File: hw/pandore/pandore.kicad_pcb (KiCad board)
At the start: 4 copper layers, 100 x 100 mm, 65 parts, among them U1 LattePanda_Mu, U2 mem_flash_spi, U3 RP2350B, U4 RP2350B, U5 mem_flash_spi, U6 mem_flash_spi

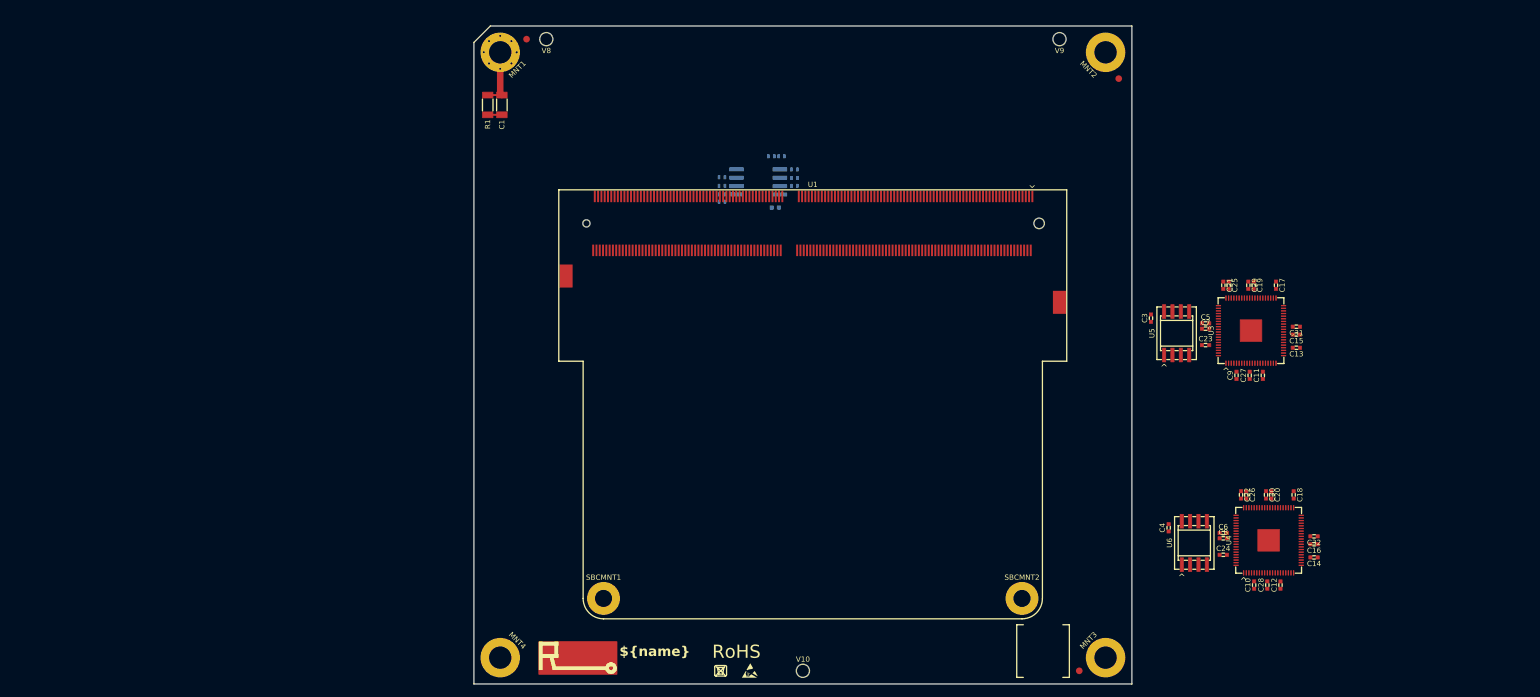
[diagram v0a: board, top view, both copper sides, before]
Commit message: added usb, hdmi and combo xlrtrs connectors resized pcb for something realistic (still wip)
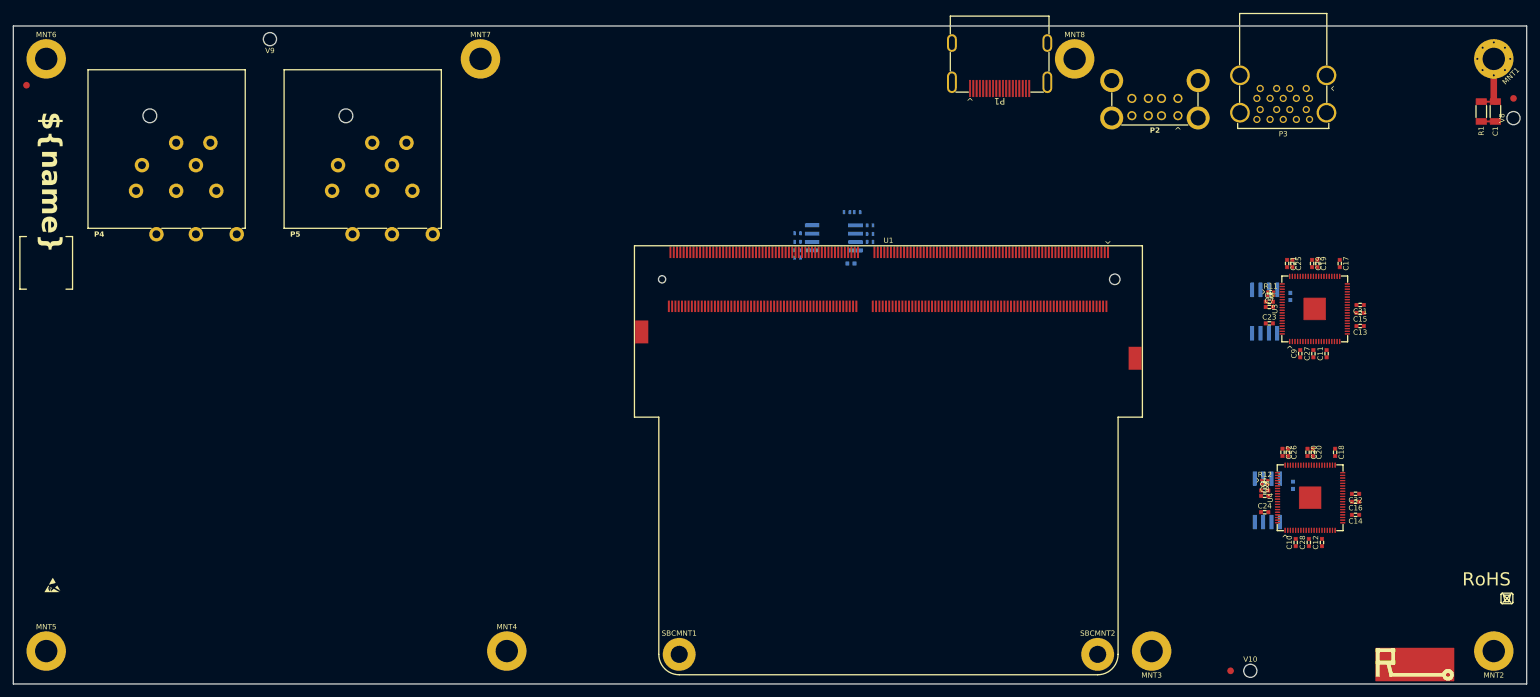
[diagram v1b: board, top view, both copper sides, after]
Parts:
- added MNT5: Mounting, reekilib_mnt:mnt_M3, F.Cu at (35.0, 145.0)
- added MNT6: Mounting, reekilib_mnt:mnt_M3, F.Cu at (35.0, 55.0)
- added MNT7: Mounting, reekilib_mnt:mnt_M3, F.Cu at (101.0, 55.0)
- added MNT8: Mounting, reekilib_mnt:mnt_M3, F.Cu at (191.3, 55.0)
- added P1: HDMI, reekilib_con:TE_1747981-1, F.Cu at (179.9, 54.6)
- added P2: USB2-A_2stacked, reekilib_con:USB2_A_RCPT_HORZ_2STACKED, F.Cu at (203.5, 58.3)
- added P3: USB3-A_2stacked, reekilib_con:USB3_A_RCPT_HORZ_2STACKED, F.Cu at (223.0, 57.5)
- added P4: XLR+TRS6.35+SW, reekilib_con:neutrik_ncj9fi-h-0, F.Cu at (54.8, 75.0)
- added P5: XLR+TRS6.35+SW, reekilib_con:neutrik_ncj9fi-h-0, F.Cu at (84.5, 75.0)
- added R11: 27Ω, 5%, 63mW, reekilib_res:RESCAXSR65P100X100X35-4, F.Cu at (221.1, 90.7)
- added R12: 27Ω, 5%, 63mW, reekilib_res:RESCAXSR65P100X100X35-4, F.Cu at (220.2, 119.3)
- C3, C4, U5, U6: moved to B.Cu
- moved V6 166.0 mm to (32.0, 59.0)
- moved V11 162.6 mm to (35.0, 86.0)
- moved C1 151.0 mm to (255.2, 63.0)
- moved MNT1 151.0 mm to (255.0, 55.0)
- moved R1 151.0 mm to (253.1, 63.0)
- moved V5 150.3 mm to (258.0, 61.0), turned to -90 degrees
- moved V8 147.5 mm to (258.0, 64.0), turned to -90 degrees
- moved V1 127.2 mm to (243.0, 147.0)
- moved V3 120.0 mm to (257.0, 137.0)
- moved V9 120.0 mm to (69.0, 52.0)
- moved V2 114.5 mm to (254.0, 134.0)
- moved MNT2 108.5 mm to (255.0, 145.0), turned to 45 degrees
- moved V4 106.8 mm to (36.0, 135.0)
- moved V10 68.0 mm to (218.0, 148.0)
- moved V7 23.0 mm to (215.0, 148.0)
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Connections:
- U3 pad 66: unconnected-(U3B-USB.D-|USB-Pad66) -> /Mgmt MCU/MCU/_USB.D-
- U3 pad 67: unconnected-(U3B-USB.D+|USB-Pad67) -> /Mgmt MCU/MCU/_USB.D+
- U4 pad 66: unconnected-(U4B-USB.D-|USB-Pad66) -> /Real-Time MCU/MCU/_USB.D-
- U4 pad 67: unconnected-(U4B-USB.D+|USB-Pad67) -> /Real-Time MCU/MCU/_USB.D+
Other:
- board size 100 x 100 mm -> 230 x 100 mm

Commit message: added RP2350's crystals added 8p8c shielded with led connector (both the same for now)
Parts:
- added J1: 8p8c_2led_shield, reekilib_con:amphenol_RJE58-188-54x1-0x, F.Cu at (160.0, 61.0)
- added J2: 8p8c_2led_shield, reekilib_con:amphenol_RJE58-188-54x1-0x, F.Cu at (140.0, 61.0)
- added X1: 12MHz, 30ppm+30ppm, 10pF, reekilib_osc:OSCCC320X250X90, F.Cu at (241.2, 97.0)
- added X2: 12MHz, 30ppm+30ppm, 10pF, reekilib_osc:OSCCC320X250X90, F.Cu at (238.2, 122.0)

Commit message: added all remaining connectors (only missing M.2 now)
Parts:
- removed P1: HDMI, reekilib_con:TE_1747981-1
- removed P2: USB2-A_2stacked, reekilib_con:USB2_A_RCPT_HORZ_2STACKED
- removed P3: USB3-A_2stacked, reekilib_con:USB3_A_RCPT_HORZ_2STACKED
- removed P4, P5: XLR+TRS6.35+SW, reekilib_con:neutrik_ncj9fi-h-0
- added J10: MIDI_in, reekilib_con:samesky_SDS-50J, F.Cu at (164.7, 57.0)
- added J11: MIDI_out, reekilib_con:samesky_SDS-50J, F.Cu at (143.9, 57.0)
- added J12: TRS, reekilib_con:neutrik_nsj12hf-1, F.Cu at (98.3, 68.7)
- added J3: USB3-A_2stacked, reekilib_con:USB3_A_RCPT_HORZ_2STACKED, F.Cu at (232.6, 57.4)
- added J4: XLR+TRS6.35+3SW, reekilib_con:neutrik_ncj9fi-h-0, F.Cu at (71.0, 73.4)
- added J5: XLR+TRS6.35+3SW, reekilib_con:neutrik_ncj9fi-h-0, F.Cu at (43.6, 73.4)
- added J6: VIN, reekilib_con:samesky_PJ-063BH, F.Cu at (265.8, 52.0)
- added J7: TRS, reekilib_con:samesky_SJ3-3508x, F.Cu at (116.0, 57.9)
- added J8: 8p8c_2led_shield, reekilib_con:amphenol_RJE58-188-54x1-0x, F.Cu at (243.1, 139.9)
- added J9: 8p8c_2led_shield, reekilib_con:amphenol_RJE58-188-54x1-0x, F.Cu at (193.2, 63.5)
- J1: value 8p8c_2led_shield -> HDMI; footprint reekilib_con:amphenol_RJE58-188-54x1-0x -> reekilib_con:te_1747981-1
- J2: value 8p8c_2led_shield -> USB2-A_2stacked; footprint reekilib_con:amphenol_RJE58-188-54x1-0x -> reekilib_con:USB2_A_RCPT_HORZ_2STACKED
- moved J2 111.3 mm to (251.2, 58.2), turned to 180 degrees
- moved J1 52.8 mm to (212.4, 54.2), turned to 90 degrees
- moved MNT7 28.0 mm to (129.0, 55.0)
- moved R1 20.0 mm to (273.1, 63.0)
- moved C1 20.0 mm to (275.2, 63.0)
- moved MNT1 20.0 mm to (275.0, 55.0)
- moved MNT2 20.0 mm to (275.0, 145.0)
- moved V1 20.0 mm to (263.0, 147.0)
- moved V2 20.0 mm to (274.0, 134.0)
- moved V3 20.0 mm to (277.0, 137.0)
- moved V5 20.0 mm to (278.0, 61.0)
- moved V8 20.0 mm to (278.0, 64.0)
- moved V9 11.7 mm to (57.3, 52.0)
- moved MNT8 11.2 mm to (180.1, 55.0)
- moved MNT5 10.0 mm to (25.0, 145.0)
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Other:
- board size 230 x 100 mm -> 260 x 100 mm
- board text added: "connector's plane"

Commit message: Added lots to sch and pcb: eth passive, audio codec, midi, teensy Corrected and added support for M.2
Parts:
- added C33: 100nF, 16V, X7R, reekilib_cap:CAPC1005, B.Cu at (237.6, 57.8)
- added C34: 100nF, 16V, X7R, reekilib_cap:CAPC1005, B.Cu at (238.4, 57.8)
- added C35: 100nF, 16V, X7R, reekilib_cap:CAPC1005, F.Cu at (232.8, 61.5)
- added C36: 100nF, 16V, X7R, reekilib_cap:CAPC1005, F.Cu at (233.5, 61.5)
- added C37: 15pF, 6.3V, X7R, reekilib_cap:CAPC1005, F.Cu at (265.0, 91.5)
- added C38: 15pF, 6.3V, X7R, reekilib_cap:CAPC1005, F.Cu at (248.7, 123.2)
- added C39: 15pF, 6.3V, X7R, reekilib_cap:CAPC1005, F.Cu at (265.0, 86.7)
- added C40: 15pF, 6.3V, X7R, reekilib_cap:CAPC1005, F.Cu at (252.1, 126.6)
- added C41: 100nF, 16V, X7R, reekilib_cap:CAPC1005, B.Cu at (157.5, 78.8)
- added C42: 100nF, 16V, X7R, reekilib_cap:CAPC1005, B.Cu at (156.7, 78.8)
- added C43: 100nF, 16V, X7R, reekilib_cap:CAPC1005, B.Cu at (206.4, 134.1)
- added C44: 100nF, 16V, X7R, reekilib_cap:CAPC1005, B.Cu at (205.6, 134.1)
- added C45: 100nF, 16V, X7R, reekilib_cap:CAPC1005, B.Cu at (154.5, 76.2)
- added C46: 100nF, 16V, X7R, reekilib_cap:CAPC1005, B.Cu at (154.5, 75.4)
- added C47: 100nF, 16V, X7R, reekilib_cap:CAPC1005, B.Cu at (203.4, 131.5)
- added C48: 100nF, 16V, X7R, reekilib_cap:CAPC1005, B.Cu at (203.4, 130.7)
- added C49: 1nF, 1000V, X7R, reekilib_cap:CAPC3216, F.Cu at (167.1, 75.2)
- added C50: 1nF, 1000V, X7R, reekilib_cap:CAPC3216, F.Cu at (216.1, 130.6)
- added C51: 100nF, 16V, X7R, reekilib_cap:CAPC1005, F.Cu at (172.8, 75.2)
- added C52: 100nF, 16V, X7R, reekilib_cap:CAPC1005, F.Cu at (221.8, 130.6)
- added C53: 100nF, 16V, X7R, reekilib_cap:CAPC1005, B.Cu at (154.9, 73.8)
- added C54: 100nF, 16V, X7R, reekilib_cap:CAPC1005, B.Cu at (203.8, 129.1)
- added C55: 100nF, 16V, X7R, reekilib_cap:CAPC1005, B.Cu at (162.1, 73.8)
- added C56: 100nF, 16V, X7R, reekilib_cap:CAPC1005, B.Cu at (211.0, 129.1)
- added C57: 100nF, 16V, X7R, reekilib_cap:CAPC1005, B.Cu at (162.1, 76.4)
- added C58: 100nF, 16V, X7R, reekilib_cap:CAPC1005, B.Cu at (211.0, 131.7)
- added C59: 100nF, 16V, X7R, reekilib_cap:CAPC1005, B.Cu at (159.1, 70.8)
- added C60: 100nF, 16V, X7R, reekilib_cap:CAPC1005, B.Cu at (208.1, 126.1)
- added C61: 100nF, 16V, X7R, reekilib_cap:CAPC1005, B.Cu at (155.5, 71.4)
- added C62: 100nF, 16V, X7R, reekilib_cap:CAPC1005, B.Cu at (204.4, 126.7)
- added C63: 4.7µF, 6.3V, X5R, reekilib_cap:CAPC1005, B.Cu at (154.5, 71.4)
- added C64: 4.7µF, 6.3V, X5R, reekilib_cap:CAPC1005, B.Cu at (203.4, 126.7)
- added C65: 4.7µF, 6.3V, X5R, reekilib_cap:CAPC1005, B.Cu at (153.4, 71.4)
- added C66: 4.7µF, 6.3V, X5R, reekilib_cap:CAPC1005, B.Cu at (202.4, 126.7)
- added C67: 100nF, 16V, X7R, reekilib_cap:CAPC1005, B.Cu at (158.7, 78.2)
- added C68: 100nF, 16V, X7R, reekilib_cap:CAPC1005, B.Cu at (207.6, 133.5)
- added C69: 100nF, 16V, X7R, reekilib_cap:CAPC1005, B.Cu at (154.9, 73.0)
- added C70: 100nF, 16V, X7R, reekilib_cap:CAPC1005, B.Cu at (203.8, 128.3)
- added C71: 100nF, 16V, X7R, reekilib_cap:CAPC1005, B.Cu at (161.1, 70.8)
- added C72: 100nF, 16V, X7R, reekilib_cap:CAPC1005, B.Cu at (210.1, 126.1)
- added C73: 12pF, 6.3V, X7R, reekilib_cap:CAPC1005, B.Cu at (159.1, 68.6)
- added C74: 12pF, 6.3V, X7R, reekilib_cap:CAPC1005, B.Cu at (154.1, 68.6)
- added C75: 12pF, 6.3V, X7R, reekilib_cap:CAPC1005, B.Cu at (208.1, 123.9)
- added C76: 12pF, 6.3V, X7R, reekilib_cap:CAPC1005, B.Cu at (203.1, 123.9)
- added C77: 100nF, 16V, X7R, reekilib_cap:CAPC1005, F.Cu at (211.4, 56.4)
- added C78: 100nF, 16V, X7R, reekilib_cap:CAPC1005, F.Cu at (212.2, 56.4)
- added C79: 100nF, 16V, X7R, reekilib_cap:CAPC1005, F.Cu at (209.1, 56.4)
- added C80: 100nF, 16V, X7R, reekilib_cap:CAPC1005, F.Cu at (209.9, 56.4)
- added C81: 100nF, 16V, X7R, reekilib_cap:CAPC1005, F.Cu at (206.8, 56.4)
- added C82: 100nF, 16V, X7R, reekilib_cap:CAPC1005, F.Cu at (207.6, 56.4)
- added C83: 100nF, 16V, X7R, reekilib_cap:CAPC1005, F.Cu at (213.8, 56.4)
- added C84: 100nF, 16V, X7R, reekilib_cap:CAPC1005, F.Cu at (214.6, 56.4)
- added C85: 100nF, 16V, X7R, reekilib_cap:CAPC1005, F.Cu at (166.0, 58.6)
- added C86: 100nF, 16V, X7R, reekilib_cap:CAPC1005, F.Cu at (164.7, 58.6)
- added C87: 100nF, 16V, X7R, reekilib_cap:CAPC1005, F.Cu at (146.6, 62.7)
- added C88: 100nF, 16V, X7R, reekilib_cap:CAPC1005, F.Cu at (74.5, 98.7)
- added C89: 10µF, 16V, X5R, reekilib_cap:CAPC2012, F.Cu at (74.7, 96.5)
- added C90: 100nF, 16V, X7R, reekilib_cap:CAPC1005, F.Cu at (74.7, 107.8)
- added C91: 100nF, 16V, X7R, reekilib_cap:CAPC1005, F.Cu at (75.6, 107.8)
- added C92: 10µF, 16V, X5R, reekilib_cap:CAPC2012, F.Cu at (75.1, 109.8)
- added C93: 100nF, 16V, X7R, reekilib_cap:CAPC1005, F.Cu at (73.0, 98.2)
- added C94: 47µF, 25V, 20%, reekilib_cap:CAPAE630Xxxx, F.Cu at (74.5, 90.8)
- added C95: 100nF, 16V, X7R, reekilib_cap:CAPC1005, F.Cu at (78.8, 98.7)
- added C96: 12pF, 6.3V, X7R, reekilib_cap:CAPC1005, F.Cu at (65.8, 106.1)
- added C97: 12pF, 6.3V, X7R, reekilib_cap:CAPC1005, F.Cu at (69.1, 109.5)
- added D1: green, reekilib_led:LEDM1608X80, B.Cu at (138.5, 117.8)
- added D10: 5V, reekilib_dfn:DFN50P100X250X55-10, F.Cu at (250.2, 59.0)
- added D11: 5V, reekilib_dfn:DFN50P100X250X55-10, F.Cu at (228.2, 58.8)
- added D12: 5V, reekilib_dfn:DFN50P100X250X55-10, F.Cu at (232.5, 58.8)
- added D13: 5V, reekilib_dfn:DFN50P100X250X55-10, F.Cu at (236.5, 58.8)
- added D14: 5V, reekilib_dfn:DFN50P100X250X55-10, F.Cu at (209.2, 53.8)
- added D15: 5V, reekilib_dfn:DFN50P100X250X55-10, F.Cu at (212.2, 53.8)
- added D16: 5V, reekilib_dfn:DFN50P100X250X55-10, F.Cu at (215.6, 53.8)
- added D17: 75V, 150mA, 1V@100mA, reekilib_sod:sod-123, F.Cu at (160.4, 63.1)
- added D18: 40V, 3A, 500mV@3A, reekilib_dio:dio_sma, B.Cu at (219.0, 63.6)
- added D2: green, reekilib_led:LEDM1608X80, B.Cu at (137.8, 85.8)
- added D3: green, reekilib_led:LEDM1608X80, B.Cu at (137.7, 87.2)
- added D4: green, reekilib_led:LEDM1608X80, F.Cu at (200.2, 61.8)
- added D5: green, reekilib_led:LEDM1608X80, F.Cu at (249.0, 130.2)
- added D6: 5V, reekilib_dfn:DFN50P100X250X55-10, F.Cu at (266.5, 130.5)
- added D7: 5V, reekilib_dfn:DFN50P100X250X55-10, F.Cu at (266.5, 127.5)
- added D8: 5V, reekilib_dfn:DFN50P100X250X55-10, F.Cu at (266.4, 107.5)
- added D9: 5V, reekilib_dfn:DFN50P100X250X55-10, F.Cu at (266.4, 104.5)
- added J13: NGFF_M.2_M, reekilib_con:NGFF_M.2_CONN, B.Cu at (141.9, 130.1)
- added J15: AIO, reekilib_con:HDR254P3X8-THRA, F.Cu at (273.4, 129.0)
- added J16: DIO, reekilib_con:HDR254P3X8-THRA, F.Cu at (273.4, 106.2)
- added J17: GROVE, reekilib_con:te_2041145-4, F.Cu at (276.6, 70.0)
- added J18: GROVE, reekilib_con:te_2041145-4, F.Cu at (276.6, 83.2)
- added J19: NGFF_M.2_AE, reekilib_con:NGFF_M.2_CONN, B.Cu at (141.9, 99.2)
- added JMP1: MIDIRX, reekilib_con:HDR254P1X03-TH, F.Cu at (137.5, 66.5)
- added JMP2: MIDITX, reekilib_con:HDR254P1X03-TH, F.Cu at (137.5, 62.5)
- added Q1: MOSFET_EN-N, reekilib_sot:SOT95P280X100-3, B.Cu at (210.7, 59.5)
- added Q2: MOSFET_EN-N, reekilib_sot:SOT95P280X100-3, B.Cu at (208.1, 64.5)
- added Q3: MOSFET_EN-N, reekilib_sot:SOT95P280X100-3, B.Cu at (211.4, 64.5)
- added Q4: MOSFET_EN-N, reekilib_sot:SOT95P280X100-3, B.Cu at (214.7, 64.5)
- added R13: 10kΩ, 1%, 63mW, reekilib_res:RESC1005, B.Cu at (135.8, 138.5)
- added R14: 1kΩ, 1%, 63mW, reekilib_res:RESC1005, B.Cu at (135.8, 136.9)
- added R15: 1kΩ, 1%, 63mW, reekilib_res:RESC1005, F.Cu at (263.0, 88.3)
- added R16: 1kΩ, 1%, 63mW, reekilib_res:RESC1005, F.Cu at (252.4, 124.0)
- added R17: 10kΩ, 1%, 63mW, reekilib_res:RESC1005, B.Cu at (152.7, 73.9)
- added R18: 10kΩ, 1%, 63mW, reekilib_res:RESC1005, B.Cu at (201.6, 129.2)
- added R19: 10kΩ, 1%, 63mW, reekilib_res:RESC1005, B.Cu at (151.7, 73.9)
- added R20: 10kΩ, 1%, 63mW, reekilib_res:RESC1005, B.Cu at (200.6, 129.2)
- added R21: 1kΩ, 1%, 63mW, reekilib_res:RESC1005, B.Cu at (140.7, 117.9)
- added R22: 1kΩ, 1%, 63mW, reekilib_res:RESC1005, B.Cu at (140.2, 85.8)
- added R23: 1kΩ, 1%, 63mW, reekilib_res:RESC1005, B.Cu at (140.0, 87.2)
- added R24: 1MΩ, 1%, 63mW, reekilib_res:RESC1005, B.Cu at (157.6, 70.6)
- added R25: 1MΩ, 1%, 63mW, reekilib_res:RESC1005, B.Cu at (206.6, 125.9)
- added R26: 2.49kΩ, 1%, 63mW, reekilib_res:RESC1005, B.Cu at (160.1, 70.8)
- added R27: 2.49kΩ, 1%, 63mW, reekilib_res:RESC1005, B.Cu at (209.1, 126.1)
- added R28: 470Ω, 1%, 63mW, reekilib_res:RESC1005, B.Cu at (199.0, 63.8)
- added R29: 470Ω, 1%, 63mW, reekilib_res:RESC1005, B.Cu at (249.0, 131.2)
- added R30: 470Ω, 1%, 63mW, reekilib_res:RESC1005, B.Cu at (200.0, 63.8)
- added R31: 470Ω, 1%, 63mW, reekilib_res:RESC1005, B.Cu at (249.0, 130.2)
- added R32: 0Ω, 5%, 63mW, reekilib_res:RESC1005, B.Cu at (183.0, 58.8)
- added R33: 0Ω, 5%, 63mW, reekilib_res:RESC1005, B.Cu at (231.1, 134.2)
- added R34: 75Ω, 1%, 250mW, reekilib_res:RESMELF0204, B.Cu at (166.6, 70.3)
- added R35: 75Ω, 1%, 250mW, reekilib_res:RESMELF0204, B.Cu at (215.5, 125.6)
- added R36: 75Ω, 1%, 250mW, reekilib_res:RESMELF0204, B.Cu at (166.6, 74.1)
- added R37: 75Ω, 1%, 250mW, reekilib_res:RESMELF0204, B.Cu at (215.5, 129.4)
- added R38: 75Ω, 1%, 250mW, reekilib_res:RESMELF0204, B.Cu at (166.6, 77.9)
- added R39: 75Ω, 1%, 250mW, reekilib_res:RESMELF0204, B.Cu at (215.5, 133.2)
- added R40: 75Ω, 1%, 250mW, reekilib_res:RESMELF0204, B.Cu at (166.6, 81.7)
- added R41: 75Ω, 1%, 250mW, reekilib_res:RESMELF0204, B.Cu at (215.5, 137.0)
- added R42: 1kΩ, 1%, 63mW, reekilib_res:RESC1005, B.Cu at (201.0, 63.8)
- added R43: 1kΩ, 1%, 63mW, reekilib_res:RESC1005, B.Cu at (249.0, 129.2)
- added R44: 560Ω, 5%, 63mW, reekilib_res:RESCAXSR50P200X100X35-8, F.Cu at (264.5, 127.5)
- added R45: 560Ω, 5%, 63mW, reekilib_res:RESCAXSR50P200X100X35-8, F.Cu at (264.4, 104.5)
- added R46: 560Ω, 5%, 63mW, reekilib_res:RESCAXSR50P200X100X35-8, F.Cu at (264.5, 130.5)
- added R47: 560Ω, 5%, 63mW, reekilib_res:RESCAXSR50P200X100X35-8, F.Cu at (264.4, 107.5)
- added R48: 0Ω, 5%, 63mW, reekilib_res:RESC1005, F.Cu at (244.8, 57.5)
- added R49: 0Ω, 5%, 63mW, reekilib_res:RESC1005, F.Cu at (225.5, 57.5)
- added R50: 0Ω, 5%, 63mW, reekilib_res:RESC1005, F.Cu at (219.8, 52.2)
- added R51: 220Ω, 1%, 250mW, reekilib_res:RESC2012, F.Cu at (160.2, 59.1)
- added R52: 10Ω, 1%, 250mW, reekilib_res:RESC2012, F.Cu at (146.0, 59.1)
- added R53: 33Ω, 1%, 250mW, reekilib_res:RESC2012, F.Cu at (138.9, 59.0)
- added R54: 0Ω, 5%, 63mW, reekilib_res:RESC1005, F.Cu at (143.9, 58.4)
- added R55: 560Ω, 5%, 63mW, reekilib_res:RESCAXSR50P200X100X35-8, B.Cu at (208.4, 57.0)
- added R56: 560Ω, 5%, 63mW, reekilib_res:RESCAXSR50P200X100X35-8, B.Cu at (213.0, 57.0)
- added R57: 2.2kΩ, 1%, 63mW, reekilib_res:RESC1005, B.Cu at (207.6, 66.7)
- added R58: 2.2kΩ, 1%, 63mW, reekilib_res:RESC1005, B.Cu at (208.6, 62.4)
- added R59: 2.2kΩ, 1%, 63mW, reekilib_res:RESC1005, B.Cu at (210.9, 66.7)
- added R60: 2.2kΩ, 1%, 63mW, reekilib_res:RESC1005, B.Cu at (212.3, 62.4)
- added R61: 2.2kΩ, 1%, 63mW, reekilib_res:RESC1005, B.Cu at (214.2, 66.7)
- added R62: 2.2kΩ, 1%, 63mW, reekilib_res:RESC1005, B.Cu at (215.6, 62.4)
- added R63: 0Ω, 5%, 63mW, reekilib_res:RESC1005, F.Cu at (79.5, 102.9)
- added R64: 10kΩ, 1%, 63mW, reekilib_res:RESC1005, F.Cu at (78.0, 107.4)
- added R65: 1kΩ, 1%, 63mW, reekilib_res:RESC1005, F.Cu at (79.6, 107.4)
- added T1: tran_choke_center, reekilib_trf:TDK_ALT3232M, B.Cu at (171.0, 69.5)
- added T10: tran_choke_center, reekilib_trf:TDK_ALT3232M, B.Cu at (220.0, 132.4)
- added T11: tran_choke_center, reekilib_trf:TDK_ALT3232M, B.Cu at (175.4, 77.7)
- added T12: tran_choke_center, reekilib_trf:TDK_ALT3232M, B.Cu at (224.4, 133.0)
- added T13: tran_choke_center, reekilib_trf:TDK_ALT3232M, B.Cu at (171.0, 80.9)
- added T14: tran_choke_center, reekilib_trf:TDK_ALT3232M, B.Cu at (220.0, 136.2)
- added T15: tran_choke_center, reekilib_trf:TDK_ALT3232M, B.Cu at (175.4, 82.1)
- added T16: tran_choke_center, reekilib_trf:TDK_ALT3232M, B.Cu at (224.4, 137.4)
- added T2: tran_choke_center, reekilib_trf:TDK_ALT3232M, B.Cu at (220.0, 124.8)
- added T3: tran_choke_center, reekilib_trf:TDK_ALT3232M, B.Cu at (175.4, 68.9)
- added T4: tran_choke_center, reekilib_trf:TDK_ALT3232M, B.Cu at (224.4, 124.2)
- added T5: tran_choke_center, reekilib_trf:TDK_ALT3232M, B.Cu at (171.0, 73.3)
- added T6: tran_choke_center, reekilib_trf:TDK_ALT3232M, B.Cu at (220.0, 128.6)
- added T7: tran_choke_center, reekilib_trf:TDK_ALT3232M, B.Cu at (175.4, 73.3)
- added T8: tran_choke_center, reekilib_trf:TDK_ALT3232M, B.Cu at (224.4, 128.6)
- added T9: tran_choke_center, reekilib_trf:TDK_ALT3232M, B.Cu at (171.0, 77.1)
- added U10: H11L1, reekilib_soic:SOIC254P1030X430-6, F.Cu at (153.1, 61.4)
- added U11: CS4272, reekilib_sop:SOP65P640X970-28, F.Cu at (73.8, 102.9)
- added U7: RTL8111H, reekilib_qfn:QFN40P400X400-33, B.Cu at (158.4, 74.4)
- added U8: RTL8111H, reekilib_qfn:QFN40P400X400-33, B.Cu at (207.4, 129.7)
- added U9: Teensy 4.1, reekilib_som:teensy_4.1, F.Cu at (65.7, 129.3)
- added X3: 25MHz, 30ppm+30ppm, 10pF, reekilib_osc:OSCCC320X250X90, B.Cu at (156.6, 68.6)
- added X4: 25MHz, 30ppm+30ppm, 10pF, reekilib_osc:OSCCC320X250X90, B.Cu at (205.6, 123.9)
- added X5: 24.576MHz, 50ppm+20ppm, 18pF, reekilib_osc:OSCCC320X250X90, F.Cu at (67.5, 107.8)
- C31, C32: value 4.7nF, 6.3V, X5R -> 4.7µF, 6.3V, X5R
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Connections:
- J1 pad 0: unconnected-(J1-SHD-Pad0) -> Net-(J1-SHD)
- J1 pad 1: unconnected-(J1-TMDS.D2+-Pad1) -> Net-(J1-TMDS.D2+)
- J1 pad 10: unconnected-(J1-TMDS.CLK+-Pad10) -> Net-(J1-TMDS.CLK+)
- J1 pad 11: unconnected-(J1-TMDS.CLKSHD-Pad11) -> VSS
- J1 pad 12: unconnected-(J1-TMDS.CLK--Pad12) -> Net-(J1-TMDS.CLK-)
- J1 pad 13: unconnected-(J1-CEC-Pad13) -> Net-(J1-CEC)
- J1 pad 15: unconnected-(J1-DDC.CLK-Pad15) -> Net-(J1-DDC.CLK)
- J1 pad 16: unconnected-(J1-DDC.DATA-Pad16) -> Net-(J1-DDC.DATA)
- J1 pad 17: unconnected-(J1-GND-Pad17) -> VSS
- J1 pad 18: unconnected-(J1-5V-Pad18) -> Net-(D18-C)
- J1 pad 19: unconnected-(J1-HotPlugDetect-Pad19) -> Net-(J1-HotPlugDetect)
- J1 pad 2: unconnected-(J1-TMDS.D2SHD-Pad2) -> VSS
- J1 pad 3: unconnected-(J1-TMDS.D2--Pad3) -> Net-(J1-TMDS.D2-)
- J1 pad 4: unconnected-(J1-TMDS.D1+-Pad4) -> Net-(J1-TMDS.D1+)
- J1 pad 5: unconnected-(J1-TMDS.D1SHD-Pad5) -> VSS
- J1 pad 6: unconnected-(J1-TMDS.D1--Pad6) -> Net-(J1-TMDS.D1-)
- J1 pad 7: unconnected-(J1-TMDS.D0+-Pad7) -> Net-(J1-TMDS.D0+)
- J1 pad 8: unconnected-(J1-TMDS.D0SHD-Pad8) -> VSS
- J1 pad 9: unconnected-(J1-TMDS.D0--Pad9) -> Net-(J1-TMDS.D0-)
- J10 pad 2: unconnected-(J10-SHIELD-Pad2) -> Net-(J10-SHIELD)
- J10 pad 4: unconnected-(J10-CSRC-Pad4) -> Net-(J10-CSRC)
- J10 pad 5: unconnected-(J10-CSINK-Pad5) -> Net-(D17-A)
- J10 pad G: unconnected-(J10-GND-PadG) -> Net-(J10-GND)
- J11 pad 2: unconnected-(J11-GND-Pad2) -> Net-(J11-GND-Pad2)
- J11 pad 4: unconnected-(J11-CSINK-Pad4) -> Net-(J11-CSINK)
- J11 pad 5: unconnected-(J11-CSRC-Pad5) -> Net-(J11-CSRC)
- J11 pad G: unconnected-(J11-GND-PadG) -> Net-(J11-GND-Pad2)
- J2 pad 2: unconnected-(J2A-TOP_D--Pad2) -> /Computer/USB2P5.D-
- J2 pad 3: unconnected-(J2A-TOP_D+-Pad3) -> /Computer/USB2P5.D+
- J2 pad 4: unconnected-(J2A-TOP_GND-Pad4) -> VSS
- J2 pad 6: unconnected-(J2B-BOT_D--Pad6) -> /Computer/USB2P3.D-
- J2 pad 7: unconnected-(J2B-BOT_D+-Pad7) -> /Computer/USB2P3.D+
- J2 pad 8: unconnected-(J2B-BOT_GND-Pad8) -> VSS
- J2 pad 9: unconnected-(J2A-SHD-Pad9) -> Net-(J2A-SHD)
- J3 pad 11: unconnected-(J3A-TOP_D--Pad11) -> /Computer/USBP1.D-
- J3 pad 12: unconnected-(J3A-TOP_D+-Pad12) -> /Computer/USBP1.D+
- J3 pad 13: unconnected-(J3A-TOP_GND-Pad13) -> VSS
- J3 pad 14: unconnected-(J3A-TOP_SSRX--Pad14) -> /Computer/USBP1.SSRX-
- J3 pad 15: unconnected-(J3A-TOP_SSRX+-Pad15) -> /Computer/USBP1.SSRX+
- J3 pad 16: unconnected-(J3A-TOP_GNDSS-Pad16) -> VSS
- J3 pad 17: unconnected-(J3A-TOP_SSTX--Pad17) -> /USB ports/_USB3HIGH.SSTX-
- J3 pad 18: unconnected-(J3A-TOP_SSTX+-Pad18) -> /USB ports/_USB3HIGH.SSTX+
- J3 pad 19: unconnected-(J3A-SHD-Pad19) -> Net-(J3A-SHD)
- J3 pad 2: unconnected-(J3B-BOT_D--Pad2) -> /Computer/USB3P2.D-
- J3 pad 3: unconnected-(J3B-BOT_D+-Pad3) -> /Computer/USB3P2.D+
- J3 pad 4: unconnected-(J3B-BOT_GND-Pad4) -> VSS
- J3 pad 5: unconnected-(J3B-BOT_SSRX--Pad5) -> /Computer/USB3P2.SSRX-
- J3 pad 6: unconnected-(J3B-BOT_SSRX+-Pad6) -> /Computer/USB3P2.SSRX+
- J3 pad 7: unconnected-(J3B-BOT_GNDSS-Pad7) -> VSS
- J3 pad 8: unconnected-(J3B-BOT_SSTX--Pad8) -> /USB ports/_USB3LOW.SSTX-
- J3 pad 9: unconnected-(J3B-BOT_SSTX+-Pad9) -> /USB ports/_USB3LOW.SSTX+
- J8 pad 1: unconnected-(J8-C1-Pad1) -> /Internal Ethernet/PAIR0+
- J8 pad 2: unconnected-(J8-C2-Pad2) -> /Internal Ethernet/PAIR0-
- J8 pad 3: unconnected-(J8-C3-Pad3) -> /Internal Ethernet/PAIR1+
- J8 pad 4: unconnected-(J8-C4-Pad4) -> /Internal Ethernet/PAIR1-
- J8 pad 5: unconnected-(J8-C5-Pad5) -> /Internal Ethernet/PAIR2+
- J8 pad 6: unconnected-(J8-C6-Pad6) -> /Internal Ethernet/PAIR2-
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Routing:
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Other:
- board size 260 x 100 mm -> 260 x 110 mm
- board text added: "TODO: change M.2s for higher Z"

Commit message: lots of work done all around
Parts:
- added C100: 10µF, 25V, X5R, reekilib_cap:CAPC2012, F.Cu at (103.8, 104.7)
- added C101: 10µF, 25V, X5R, reekilib_cap:CAPC2012, F.Cu at (110.2, 99.0)
- added C102: 10µF, 25V, X5R, reekilib_cap:CAPC2012, F.Cu at (100.0, 106.5)
- added C103: 4.7µF, 6.3V, X5R, reekilib_cap:CAPC1005, F.Cu at (92.8, 107.5)
- added C104: 47µF, 25V, 20%, reekilib_cap:CAPAE630Xxxx, F.Cu at (104.8, 100.2)
- added C105: 100pF, 1kV, X5R, reekilib_cap:CAPC3216, F.Cu at (97.2, 111.5)
- added C106: 100pF, 1kV, X5R, reekilib_cap:CAPC3216, B.Cu at (27.5, 111.5)
- added C107: 100pF, 1kV, X5R, reekilib_cap:CAPC3216, F.Cu at (27.5, 111.5)
- added C108: 100pF, 1kV, X5R, reekilib_cap:CAPC3216, F.Cu at (125.8, 96.8)
- added C109: 100pF, 1kV, X5R, reekilib_cap:CAPC3216, B.Cu at (112.0, 111.5)
- added C110: 47µF, 25V, 20%, reekilib_cap:CAPAE630Xxxx, F.Cu at (117.8, 122.2)
- added C111: 10µF, 25V, X5R, reekilib_cap:CAPC2012, F.Cu at (116.0, 94.2)
- added C112: 10µF, 25V, X5R, reekilib_cap:CAPC2012, F.Cu at (113.2, 92.5)
- added C113: 100nF, 16V, X7R, reekilib_cap:CAPC1005, F.Cu at (117.2, 99.8)
- added C114: 100nF, 16V, X7R, reekilib_cap:CAPC1005, F.Cu at (92.8, 105.5)
- added C115: 100nF, 16V, X7R, reekilib_cap:CAPC1005, F.Cu at (104.2, 109.0)
- added C116: 100nF, 16V, X7R, reekilib_cap:CAPC1005, F.Cu at (119.2, 113.0)
- added C117: 1.3nF, 16V, C0G, reekilib_cap:CAPC1608, B.Cu at (46.5, 87.5)
- added C118: 1.3nF, 16V, C0G, reekilib_cap:CAPC1608, B.Cu at (43.5, 87.5)
- added C119: 100nF, 16V, X7R, reekilib_cap:CAPC1005, B.Cu at (41.2, 82.2)
- added C120: 10µF, 25V, X5R, reekilib_cap:CAPC2012, F.Cu at (45.0, 83.2)
- added C121: 220nF, 16V, X7R, reekilib_cap:CAPC1005, B.Cu at (41.2, 84.2)
- added C122: 100µF, 25V, 20%, reekilib_cap:CAPAE630Xxxx, F.Cu at (49.5, 76.0)
- added C123: 300pF, 16V, C0G, reekilib_cap:CAPC1608, B.Cu at (43.2, 80.8)
- added C124: 300pF, 16V, C0G, reekilib_cap:CAPC1608, B.Cu at (46.8, 80.8)
- added C125: 33nF, 16V, C0G, reekilib_cap:CAPC1608, B.Cu at (46.5, 76.0)
- added C126: 33nF, 16V, C0G, reekilib_cap:CAPC1608, B.Cu at (43.8, 76.0)
- added C127: 100µF, 25V, 20%, reekilib_cap:CAPAE630Xxxx, F.Cu at (42.2, 76.0)
- added C128: 1.3nF, 16V, C0G, reekilib_cap:CAPC1608, B.Cu at (60.0, 87.5)
- added C129: 1.3nF, 16V, C0G, reekilib_cap:CAPC1608, B.Cu at (63.0, 87.5)
- added C130: 220nF, 16V, X7R, reekilib_cap:CAPC1005, B.Cu at (57.8, 84.2)
- added C131: 300pF, 16V, C0G, reekilib_cap:CAPC1608, B.Cu at (59.8, 80.8)
- added C132: 300pF, 16V, C0G, reekilib_cap:CAPC1608, B.Cu at (63.2, 80.8)
- added C133: 100nF, 16V, X7R, reekilib_cap:CAPC1005, B.Cu at (57.8, 82.2)
- added C134: 10µF, 25V, X5R, reekilib_cap:CAPC2012, F.Cu at (61.5, 83.2)
- added C135: 33nF, 16V, C0G, reekilib_cap:CAPC1608, B.Cu at (60.2, 76.0)
- added C136: 33nF, 16V, C0G, reekilib_cap:CAPC1608, B.Cu at (63.0, 76.0)
- added C137: 100µF, 25V, 20%, reekilib_cap:CAPAE630Xxxx, F.Cu at (64.0, 76.0)
- added C138: 100µF, 25V, 20%, reekilib_cap:CAPAE630Xxxx, F.Cu at (56.8, 76.0)
- added C139: 100pF, 50V, C0G, reekilib_cap:CAPC1608, B.Cu at (105.5, 74.8)
- added C140: 100nF, 16V, X7R, reekilib_cap:CAPC1005, B.Cu at (115.2, 83.8)
- added C141: 220nF, 16V, X7R, reekilib_cap:CAPC1005, B.Cu at (115.2, 82.8)
- added C142: 1nF, 16V, C0G, reekilib_cap:CAPC1608, B.Cu at (112.5, 85.8)
- added C143: 1nF, 16V, C0G, reekilib_cap:CAPC1608, B.Cu at (109.5, 85.8)
- added C144: 100pF, 50V, C0G, reekilib_cap:CAPC1608, B.Cu at (112.5, 88.8)
- added C145: 100pF, 50V, C0G, reekilib_cap:CAPC1608, B.Cu at (109.5, 88.8)
- added C146: 100pF, 50V, C0G, reekilib_cap:CAPC1608, B.Cu at (76.5, 74.8)
- added C147: 100pF, 50V, C0G, reekilib_cap:CAPC1608, B.Cu at (73.2, 74.8)
- added C148: 220nF, 16V, X7R, reekilib_cap:CAPC1005, B.Cu at (85.2, 82.8)
- added C149: 1nF, 16V, C0G, reekilib_cap:CAPC1608, B.Cu at (82.5, 85.8)
- added C150: 1nF, 16V, C0G, reekilib_cap:CAPC1608, B.Cu at (79.5, 85.8)
- added C151: 100pF, 50V, C0G, reekilib_cap:CAPC1608, B.Cu at (82.5, 88.8)
- added C152: 100pF, 50V, C0G, reekilib_cap:CAPC1608, B.Cu at (79.5, 88.8)
- added C153: 2.7nF, 16V, C0G, reekilib_cap:CAPC1608, B.Cu at (111.0, 90.0)
- added C154: 2.7nF, 16V, C0G, reekilib_cap:CAPC1608, B.Cu at (81.0, 90.0)
- added C155: 10µF, 25V, X5R, reekilib_cap:CAPC2012, F.Cu at (111.0, 84.5)
- added C156: 100nF, 16V, X7R, reekilib_cap:CAPC1005, B.Cu at (85.2, 83.8)
- added C157: 10µF, 25V, X5R, reekilib_cap:CAPC2012, F.Cu at (81.0, 84.4)
- added C158: 100pF, 50V, C0G, reekilib_cap:CAPC1608, B.Cu at (102.2, 74.8)
- added C159: 100µF, 25V, 20%, reekilib_cap:CAPAE630Xxxx, F.Cu at (122.0, 76.0)
- added C160: 100µF, 25V, 20%, reekilib_cap:CAPAE630Xxxx, F.Cu at (114.8, 76.0)
- added C161: 100µF, 25V, 20%, reekilib_cap:CAPAE630Xxxx, F.Cu at (93.0, 76.0)
- added C162: 100µF, 25V, 20%, reekilib_cap:CAPAE630Xxxx, F.Cu at (85.8, 76.0)
- added C163: 47µF, 100V, 20%, reekilib_cap:CAPAE630Xxxx, F.Cu at (107.5, 76.0)
- added C164: 47µF, 100V, 20%, reekilib_cap:CAPAE630Xxxx, F.Cu at (100.2, 76.0)
- added C165: 47µF, 100V, 20%, reekilib_cap:CAPAE630Xxxx, F.Cu at (78.5, 76.0)
- added C166: 47µF, 100V, 20%, reekilib_cap:CAPAE630Xxxx, F.Cu at (71.2, 76.0)
- added C167: 100pF, 50V, C0G, reekilib_cap:CAPC1608, B.Cu at (88.0, 75.2)
- added C168: 100pF, 50V, C0G, reekilib_cap:CAPC1608, B.Cu at (91.0, 75.2)
- added C169: 100pF, 50V, C0G, reekilib_cap:CAPC1608, B.Cu at (89.5, 75.2)
- added C170: 100pF, 50V, C0G, reekilib_cap:CAPC1608, B.Cu at (117.0, 75.8)
- added C171: 100pF, 50V, C0G, reekilib_cap:CAPC1608, B.Cu at (118.4, 75.8)
- added C172: 100pF, 50V, C0G, reekilib_cap:CAPC1608, B.Cu at (119.8, 75.8)
- added C173: 100pF, 50V, C0G, reekilib_cap:CAPC1608, B.Cu at (111.0, 80.8)
- added C174: 100pF, 50V, C0G, reekilib_cap:CAPC1608, B.Cu at (81.0, 80.8)
- added C175: 100nF, 16V, X7R, reekilib_cap:CAPC1005, F.Cu at (114.7, 83.3)
- added C176: 100nF, 16V, X7R, reekilib_cap:CAPC1005, F.Cu at (84.7, 83.3)
- added C177: 100nF, 16V, X7R, reekilib_cap:CAPC1005, F.Cu at (42.8, 83.2)
- added C178: 100nF, 16V, X7R, reekilib_cap:CAPC1005, F.Cu at (59.0, 83.2)
- added C98: 4.7µF, 6.3V, X5R, reekilib_cap:CAPC1005, F.Cu at (117.2, 97.8)
- added C99: 10µF, 25V, X5R, reekilib_cap:CAPC2012, F.Cu at (119.8, 117.5)
- added D19: 75V, 140mA, 1.25V@150mA, reekilib_sot:SOT65P210X90-3, F.Cu at (112.3, 82.0)
- added D20: 75V, 140mA, 1.25V@150mA, reekilib_sot:SOT65P210X90-3, F.Cu at (82.3, 82.0)
- added D21: 75V, 140mA, 1.25V@150mA, reekilib_sot:SOT65P210X90-3, F.Cu at (109.6, 82.0)
- added D22: 75V, 140mA, 1.25V@150mA, reekilib_sot:SOT65P210X90-3, F.Cu at (79.6, 82.0)
- added L1: 10µH, reekilib_ind:INDC2520, F.Cu at (103.8, 107.0)
- added L2: 10µH, reekilib_ind:INDC2520, F.Cu at (119.8, 115.2)
- added L3: 10µH, reekilib_ind:INDC2520, F.Cu at (113.2, 94.8)
- added R100: 1kΩ, 0.5%, thin film, reekilib_res:RESC2012, B.Cu at (83.8, 80.8)
- added R101: 1kΩ, 0.5%, thin film, reekilib_res:RESC2012, B.Cu at (78.2, 80.8)
- added R102: 1kΩ, 0.5%, thin film, reekilib_res:RESC2012, B.Cu at (85.5, 86.0)
- added R103: 1kΩ, 0.5%, thin film, reekilib_res:RESC2012, B.Cu at (76.5, 86.0)
- added R104: 40.2Ω, 1%, thin film, reekilib_res:RESC2012, B.Cu at (82.5, 87.2)
- added R105: 40.2Ω, 1%, thin film, reekilib_res:RESC2012, B.Cu at (79.5, 87.2)
- added R106: 10kΩ, 1%, 63mW, reekilib_res:RESC1005, B.Cu at (67.2, 102.6)
- added R107: 10kΩ, 1%, 63mW, reekilib_res:RESC1005, B.Cu at (68.9, 102.6)
- added R108: 10kΩ, 1%, 63mW, reekilib_res:RESC1005, B.Cu at (67.2, 101.1)
- added R109: 10kΩ, 1%, 63mW, reekilib_res:RESC1005, B.Cu at (68.9, 101.1)
- added R110: 9.09kΩ, 0.5%, thin film, reekilib_res:RESC2012, B.Cu at (112.0, 78.5)
- added R111: 9.01kΩ, 0.5%, thin film, reekilib_res:RESC2012, B.Cu at (110.0, 78.5)
- added R112: 9.09kΩ, 0.5%, thin film, reekilib_res:RESC2012, B.Cu at (82.0, 78.5)
- added R113: 9.01kΩ, 0.5%, thin film, reekilib_res:RESC2012, B.Cu at (80.0, 78.5)
- added R114: 47kΩ, 0.5%, thin film, reekilib_res:RESC2012, B.Cu at (112.0, 75.5)
- added R115: 47kΩ, 0.5%, thin film, reekilib_res:RESC2012, B.Cu at (82.0, 75.5)
- added R116: 47kΩ, 0.5%, thin film, reekilib_res:RESC2012, B.Cu at (110.0, 75.5)
- added R117: 47kΩ, 0.5%, thin film, reekilib_res:RESC2012, B.Cu at (80.0, 75.5)
- added R118: 1kΩ, 0.5%, thin film, reekilib_res:RESC2012, B.Cu at (115.5, 78.5)
- added R119: 1kΩ, 0.5%, thin film, reekilib_res:RESC2012, B.Cu at (85.5, 78.5)
- added R120: 1kΩ, 0.5%, thin film, reekilib_res:RESC2012, B.Cu at (106.5, 78.5)
- added R121: 1kΩ, 0.5%, thin film, reekilib_res:RESC2012, B.Cu at (76.5, 78.5)
- added R122: 6.8kΩ, 0.5%, thin film, reekilib_res:RESC2012, F.Cu at (105.5, 81.8)
- added R123: 6.8kΩ, 0.5%, thin film, reekilib_res:RESC2012, F.Cu at (102.2, 81.8)
- added R124: 6.8kΩ, 0.5%, thin film, reekilib_res:RESC2012, F.Cu at (76.5, 81.8)
- added R125: 6.8kΩ, 0.5%, thin film, reekilib_res:RESC2012, F.Cu at (73.2, 81.8)
- added R66: 10kΩ, 1%, 63mW, reekilib_res:RESC1005, F.Cu at (110.7, 101.8)
- added R67: 10kΩ, 1%, 63mW, reekilib_res:RESC1005, F.Cu at (110.8, 103.2)
- added R68: 10kΩ, 1%, 63mW, reekilib_res:RESC1005, F.Cu at (117.2, 101.8)
- added R69: 10kΩ, 1%, 63mW, reekilib_res:RESC1005, F.Cu at (117.2, 103.2)
- added R70: 10kΩ, 1%, 63mW, reekilib_res:RESC1005, F.Cu at (99.8, 103.6)
- added R71: 10kΩ, 1%, 63mW, reekilib_res:RESC1005, F.Cu at (99.8, 102.1)
- added R72: 10kΩ, 1%, 63mW, reekilib_res:RESC1005, F.Cu at (92.8, 103.6)
- added R73: 10kΩ, 1%, 63mW, reekilib_res:RESC1005, F.Cu at (92.8, 102.1)
- added R74: 5.1kΩ, 0.5%, thin film, reekilib_res:RESC2012, B.Cu at (43.5, 86.0)
- added R75: 5.1kΩ, 0.5%, thin film, reekilib_res:RESC2012, B.Cu at (46.5, 86.0)
- added R76: 5.1kΩ, 0.5%, thin film, reekilib_res:RESC2012, B.Cu at (43.5, 89.2)
- added R77: 5.1kΩ, 0.5%, thin film, reekilib_res:RESC2012, B.Cu at (46.5, 89.2)
- added R78: 5.1kΩ, 0.5%, thin film, reekilib_res:RESC2012, B.Cu at (43.5, 79.2)
- added R79: 5.1kΩ, 0.5%, thin film, reekilib_res:RESC2012, B.Cu at (46.8, 79.2)
- added R80: 100Ω, 1%, thin film, reekilib_res:RESC2012, B.Cu at (43.5, 77.5)
- added R81: 100Ω, 1%, thin film, reekilib_res:RESC2012, B.Cu at (46.8, 77.5)
- added R82: 10Ω, 1%, thin film, reekilib_res:RESC2012, B.Cu at (113.8, 78.5)
- added R83: 10Ω, 1%, thin film, reekilib_res:RESC2012, B.Cu at (108.2, 78.5)
- added R84: 5.1kΩ, 0.5%, thin film, reekilib_res:RESC2012, B.Cu at (60.0, 89.2)
- added R85: 5.1kΩ, 0.5%, thin film, reekilib_res:RESC2012, B.Cu at (63.0, 89.2)
- added R86: 5.1kΩ, 0.5%, thin film, reekilib_res:RESC2012, B.Cu at (60.0, 86.0)
- added R87: 5.1kΩ, 0.5%, thin film, reekilib_res:RESC2012, B.Cu at (63.0, 86.0)
- added R88: 10Ω, 1%, thin film, reekilib_res:RESC2012, B.Cu at (83.8, 78.5)
- added R89: 10Ω, 1%, thin film, reekilib_res:RESC2012, B.Cu at (78.2, 78.5)
- added R90: 5.1kΩ, 0.5%, thin film, reekilib_res:RESC2012, B.Cu at (60.0, 79.2)
- added R91: 5.1kΩ, 0.5%, thin film, reekilib_res:RESC2012, B.Cu at (63.2, 79.2)
- added R92: 100Ω, 1%, thin film, reekilib_res:RESC2012, B.Cu at (60.0, 77.5)
- added R93: 100Ω, 1%, thin film, reekilib_res:RESC2012, B.Cu at (63.2, 77.5)
- added R94: 1kΩ, 0.5%, thin film, reekilib_res:RESC2012, B.Cu at (113.8, 80.8)
- added R95: 1kΩ, 0.5%, thin film, reekilib_res:RESC2012, B.Cu at (108.2, 80.8)
- added R96: 1kΩ, 0.5%, thin film, reekilib_res:RESC2012, B.Cu at (115.5, 86.0)
- added R97: 1kΩ, 0.5%, thin film, reekilib_res:RESC2012, B.Cu at (106.5, 86.0)
- added R98: 40.2Ω, 1%, thin film, reekilib_res:RESC2012, B.Cu at (112.5, 87.3)
- added R99: 40.2Ω, 1%, thin film, reekilib_res:RESC2012, B.Cu at (109.5, 87.3)
- added U12: NXES2, reekilib_som:murata_nxe2, F.Cu at (112.0, 111.5)
- added U13: -, reekilib_soic:SOIC127P600X150-8, F.Cu at (114.0, 100.2)
- added U14: -, reekilib_soic:SOIC127P600X150-8, F.Cu at (96.2, 104.8)
- added U15: OPAMP_DIFF_1, reekilib_sop:SOP65P490X300-8, B.Cu at (45.0, 83.2)
- added U16: OPAMP_DIFF_1, reekilib_sop:SOP65P490X300-8, B.Cu at (61.5, 83.2)
- added U17: OPAMP_DIFF_1, reekilib_sop:SOP65P490X300-8, B.Cu at (111.0, 83.3)
- added U18: OPAMP_DIFF_1, reekilib_sop:SOP65P490X300-8, B.Cu at (81.0, 83.2)
- moved C94 4.53 mm to (70.0, 90.8)
- moved C97 3.82 mm to (65.3, 109.1)
- moved C95 3.82 mm to (75.0, 98.3)
- moved C96 3.82 mm to (62.0, 105.7)
- moved X5 3.82 mm to (63.7, 107.4)
- moved C89 3.82 mm to (70.9, 96.1)
- moved C90 3.82 mm to (70.9, 107.4)
- moved C91 3.82 mm to (71.8, 107.4)
- moved C92 3.82 mm to (71.3, 109.4)
- moved U11 3.82 mm to (70.0, 102.5)
- moved C88 3.82 mm to (70.7, 98.3)
- moved C93 3.82 mm to (69.2, 97.8)
- moved R63 3.82 mm to (75.7, 102.5)
- moved R64 3.82 mm to (74.2, 107.0)
- moved R65 3.82 mm to (75.8, 107.0)
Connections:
- net Net-(U11-VA) renamed AV5
- net Net-(U11-VCOM) renamed /Audio/Audio inputs/VCM
- C90 pad 1: VSS -> VSSISO
- C90 pad 2: AVIO -> AV3P3
- C91 pad 1: VSS -> VSSISO
- C91 pad 2: AVIO -> AV3P3
- C92 pad 1: VSS -> VSSISO
- C92 pad 2: AVIO -> AV3P3
- C96 pad 1: VSS -> VSSISO
- C97 pad 1: VSS -> VSSISO
- J12 pad G: unconnected-(J12-PadG) -> AVSS
- J12 pad RB: unconnected-(J12-PadRB) -> /Audio/Audio outputs/OUTL.SIG-
- J12 pad RT: unconnected-(J12-PadRT) -> /Audio/Audio outputs/OUTR.SIG-
- J12 pad SB: unconnected-(J12-PadSB) -> /Audio/Audio outputs/OUTL.SIG+
- J12 pad ST: unconnected-(J12-PadST) -> /Audio/Audio outputs/OUTR.SIG+
- J12 pad TB: unconnected-(J12-PadTB) -> AVSS
- J12 pad TT: unconnected-(J12-PadTT) -> AVSS
- J4 pad 1: unconnected-(J4-Pad1) -> AVSS
- J4 pad 2: unconnected-(J4-Pad2) -> /Audio/Audio inputs/_MIC1IN.SIG+
- J4 pad 3: unconnected-(J4-Pad3) -> /Audio/Audio inputs/_MIC1IN.SIG-
- J4 pad G: unconnected-(J4-PadG) -> AVSS
- J4 pad R: unconnected-(J4-PadR) -> /Audio/Audio inputs/_LINE1IN.SIG-
- J4 pad S: unconnected-(J4-PadS) -> AVSS
- J4 pad T: unconnected-(J4-PadT) -> /Audio/Audio inputs/_LINE1IN.SIG+
- J5 pad 1: unconnected-(J5-Pad1) -> AVSS
- J5 pad 2: unconnected-(J5-Pad2) -> /Audio/Audio inputs/_MIC2IN.SIG+
- J5 pad 3: unconnected-(J5-Pad3) -> /Audio/Audio inputs/_MIC2IN.SIG-
- J5 pad G: unconnected-(J5-PadG) -> AVSS
- J5 pad R: unconnected-(J5-PadR) -> /Audio/Audio inputs/_LINE2IN.SIG-
- J5 pad S: unconnected-(J5-PadS) -> AVSS
- J5 pad T: unconnected-(J5-PadT) -> /Audio/Audio inputs/_LINE2IN.SIG+
- R63 pad 2: VSS -> VSSISO
- R65 pad 2: VSS -> VSSISO
- U11 pad 10: AVIO -> AV3P3
- U11 pad 23: /Audio/Audio outputs/~{MUTE}.L -> /Audio/Audio inputs/~{MUTE}.L
- U11 pad 28: /Audio/Audio outputs/~{MUTE}.R -> /Audio/Audio inputs/~{MUTE}.R
- U11 pad 8: VSS -> VSSISO
- U11 pad 9: AVIO -> AV3P3
- X5 pad 2: VSS -> VSSISO
- X5 pad 4: VSS -> VSSISO
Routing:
- net AVSS: track 0.00 -> 27.9 mm, vias 0 -> 10
- net /Audio/Audio inputs/_LINE1IN.SIG+: track 0.00 -> 27.3 mm, vias 0 -> 1
- net /Audio/Audio inputs/_LINE1IN.SIG-: track 0.00 -> 27.2 mm, vias 0 -> 1
- net /Audio/Audio inputs/_MIC2IN.SIG+: track 0.00 -> 26.0 mm, vias 0 -> 1
- net /Audio/Audio inputs/_MIC2IN.SIG-: track 0.00 -> 26.0 mm, vias 0 -> 1
- net /Audio/Audio inputs/_LINE2IN.SIG-: track 0.00 -> 25.3 mm, vias 0 -> 1
- net /Audio/Audio inputs/_LINE2IN.SIG+: track 0.00 -> 25.2 mm, vias 0 -> 1
- net /Audio/Audio inputs/_MIC1IN.SIG+: track 0.00 -> 24.6 mm, vias 0 -> 1
- net /Audio/Audio inputs/_MIC1IN.SIG-: track 0.00 -> 24.6 mm, vias 0 -> 1
- net AV5: track 0.00 -> 20.0 mm, vias 0 -> 2
- net /Audio/Audio inputs/LINE2IN.SIG+: track 0.00 -> 13.3 mm, vias 0 -> 1
- net /Audio/Audio inputs/LINE1IN.SIG+: track 0.00 -> 13.2 mm, vias 0 -> 1
- net /Audio/Audio inputs/IN buffer 1/INBUF.FB-: track 0.00 -> 12.5 mm
- net /Audio/Audio inputs/IN buffer 2/INBUF.FB-: track 0.00 -> 12.4 mm
- net /Audio/Audio inputs/IN buffer 1/INBUF.FB+: track 0.00 -> 12.3 mm
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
